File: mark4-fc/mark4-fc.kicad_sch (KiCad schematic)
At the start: 0 parts

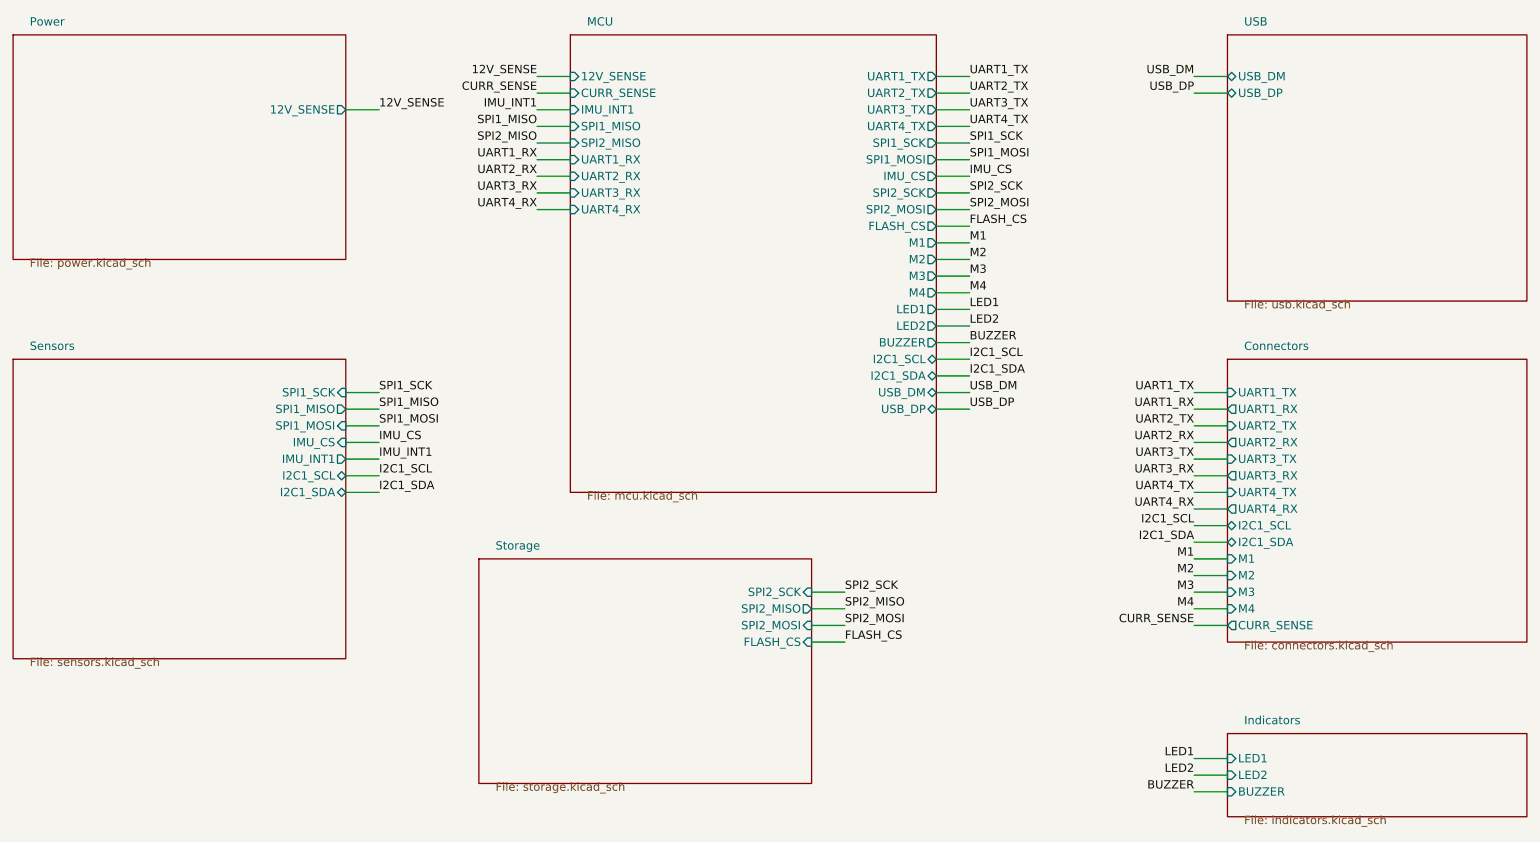
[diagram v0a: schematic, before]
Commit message: feat(hardware): shrink mark4-fc to 36x36 and split assembly by side
Board outline, connectors and assembly strategy all move in one pass;
schematic, PCB and the fab package are propagated together.

- Rebuild the Edge.Cuts outline at 36x36 (the floor the 30.5 mm M3
  pattern allows) and fix the four corner fillets whose arc midpoints
  sat diametrically opposite, which cut a 4 mm disc out of each corner.
- Reduce SWD from 6 to 3 positions (SWDIO/SWCLK/GND) so SWD plus USB-C
  fit the edge budget; SWO is gone, BOOT0 stays the recovery path.
- Move the hand-soldered parts (LDO, flash, Q1, JP1, test points and
  their pull-ups) to the bottom face; the JLCPCB package now covers the
  top side only (CPL 63 -> 52, BOM 31 -> 26 lines).
- Re-relax the placement into the smaller outline with the electrically
  critical groups hand-anchored (crystal, VCAP, buck corner, connector
  ESD); LED strip pads move to the left edge to clear the USB row.
  DRC clean, schematic parity 0, nothing routed yet.
- Hide top-silk refdes and values in favour of pad labels, add the
  orientation arrow (direction still to confirm against the frame).
- Replace the footprint-family CPL rotation table with measured,
  LCSC-keyed corrections (jlcpcb-cpl-rotations.csv), derived from the
  EasyEDA footprints; fixes U2, U1 and Q1 which the community table got
  wrong or missed.
- Correct the STO-2 flash substitution note: no 256 Mbit Winbond exists
  in SOIC-8 208 mil; list the real drop-ins and the EN4B firmware cost.

Co-Authored-By: Claude Fable 5 <noreply@anthropic.com>
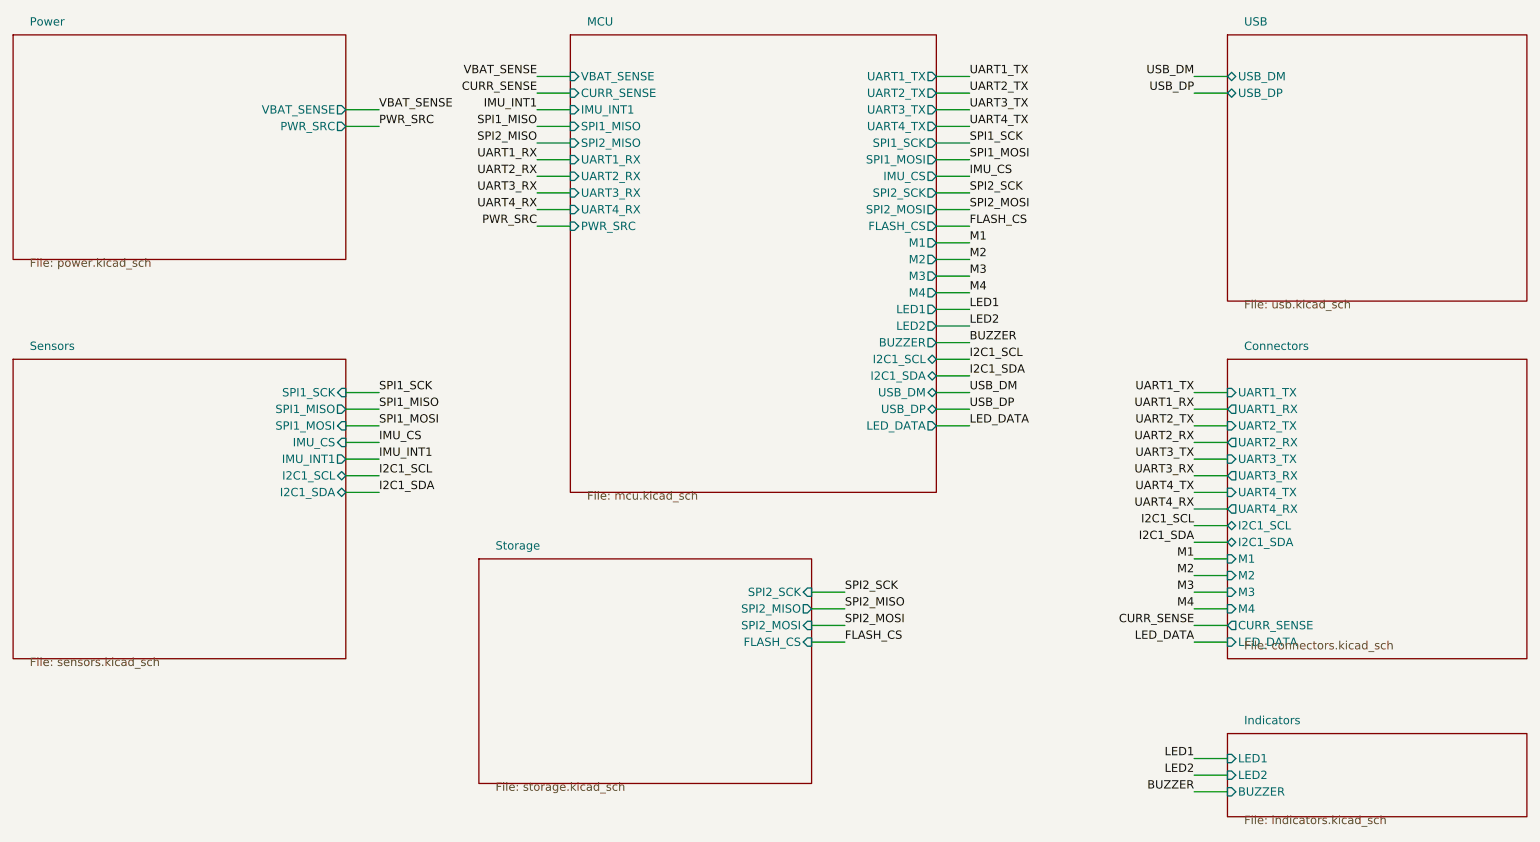
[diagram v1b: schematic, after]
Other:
- sheet Connectors ports: added LED_DATA; removed none
- sheet MCU ports: added LED_DATA, PWR_SRC, VBAT_SENSE; removed 12V_SENSE
- sheet Power ports: added PWR_SRC, VBAT_SENSE; removed 12V_SENSE
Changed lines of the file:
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@@
+	(wire
+		(pts
+			(xy 90.17 53.34) (xy 95.25 53.34)
+		)
+		(stroke
+			(width 0)
+			(type default)
+		)
+	)
+	(wire
+		(pts
+			(xy 124.46 68.58) (xy 119.38 68.58)
+		)
+		(stroke
+			(width 0)
+			(type default)
+		)
+	)
+	(wire
+		(pts
+			(xy 180.34 99.06) (xy 185.42 99.06)
+		)
+		(stroke
+			(width 0)
+			(type default)
+		)
+	)
+	(wire
+		(pts
+			(xy 224.79 132.08) (xy 219.71 132.08)
+		)
+		(stroke
+			(width 0)
+			(type default)
+		)
+	)
 	(wire
 		(pts
@@
 		)
 	)
-	(label "12V_SENSE"
+	(label "VBAT_SENSE"
 		(at 95.25 50.8 0)
 		(effects
@@
 		)
 	)
-	(label "12V_SENSE"
+	(label "VBAT_SENSE"
 		(at 119.38 45.72 180)
 		(effects
@@
 			)
 			(justify left bottom)
+		)
+	)
+	(label "PWR_SRC"
+		(at 95.25 53.34 0)
+		(effects
+			(font
+				(size 1.27 1.27)
+			)
+			(justify left bottom)
+		)
+	)
+	(label "PWR_SRC"
+		(at 119.38 68.58 180)
+		(effects
+			(font
+				(size 1.27 1.27)
+			)
+			(justify right bottom)
+		)
+	)
+	(label "LED_DATA"
+		(at 185.42 99.06 0)
+		(effects
+			(font
+				(size 1.27 1.27)
+			)
+			(justify left bottom)
+		)
+	)
+	(label "LED_DATA"
+		(at 219.71 132.08 180)
+		(effects
+			(font
+				(size 1.27 1.27)
+			)
+			(justify right bottom)
 		)
 	)
@@
 	(sheet
 		(at 224.79 88.9)
-		(size 45.72 43.18)
+		(size 45.72 45.72)
 		(exclude_from_sim no)
 		(in_bom yes)
@@
 		(pin "CURR_SENSE" output
 			(at 224.79 129.54 180)
+			(effects
+				(font
+					(size 1.27 1.27)
+				)
+				(justify left)
+			)
+		)
+		(pin "LED_DATA" input
+			(at 224.79 132.08 180)
 			(effects
 				(font
@@
 			)
 		)
-		(pin "12V_SENSE" output
+		(pin "VBAT_SENSE" output
 			(at 90.17 50.8 0)
+			(effects
+				(font
+					(size 1.27 1.27)
+				)
+				(justify right)
+			)
+		)
+		(pin "PWR_SRC" output
+			(at 90.17 53.34 0)
 			(effects
 				(font
@@
 			)
 		)
-		(pin "12V_SENSE" input
+		(pin "VBAT_SENSE" input
 			(at 124.46 45.72 180)
 			(effects
@@
 			(effects
 				(font
+					(size 1.27 1.27)
+				)
+				(justify right)
+			)
+		)
+		(pin "PWR_SRC" input
+			(at 124.46 68.58 180)
+			(effects
+				(font
+					(size 1.27 1.27)
+				)
+				(justify left)
+			)
+		)
+		(pin "LED_DATA" output
+			(at 180.34 99.06 0)
+			(effects
+				(font
